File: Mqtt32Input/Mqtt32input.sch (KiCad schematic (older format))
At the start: 66 parts, among them J1 INPUT 0-7, J10 SLAVE2 IN/DATA OUTPUT, J2 JP OPT1, J3 JP OPT2, J4 INPUT 8-15, J5 INPUT 16-23, J6 SLAVE1IN/CHAIN INPUT, J7 JP CHAIN IN(1)/SLAVE1(3), J8 JP DATA OUT(1)/SLAVE2(3), J9 INPUT 24-31, SW1 DIP NODE 0-3, SW2 DIP # Chain length, U1 74HC165, U2 74HC165, U3 74HC165, U4 74HC165, X1 0V - 5V

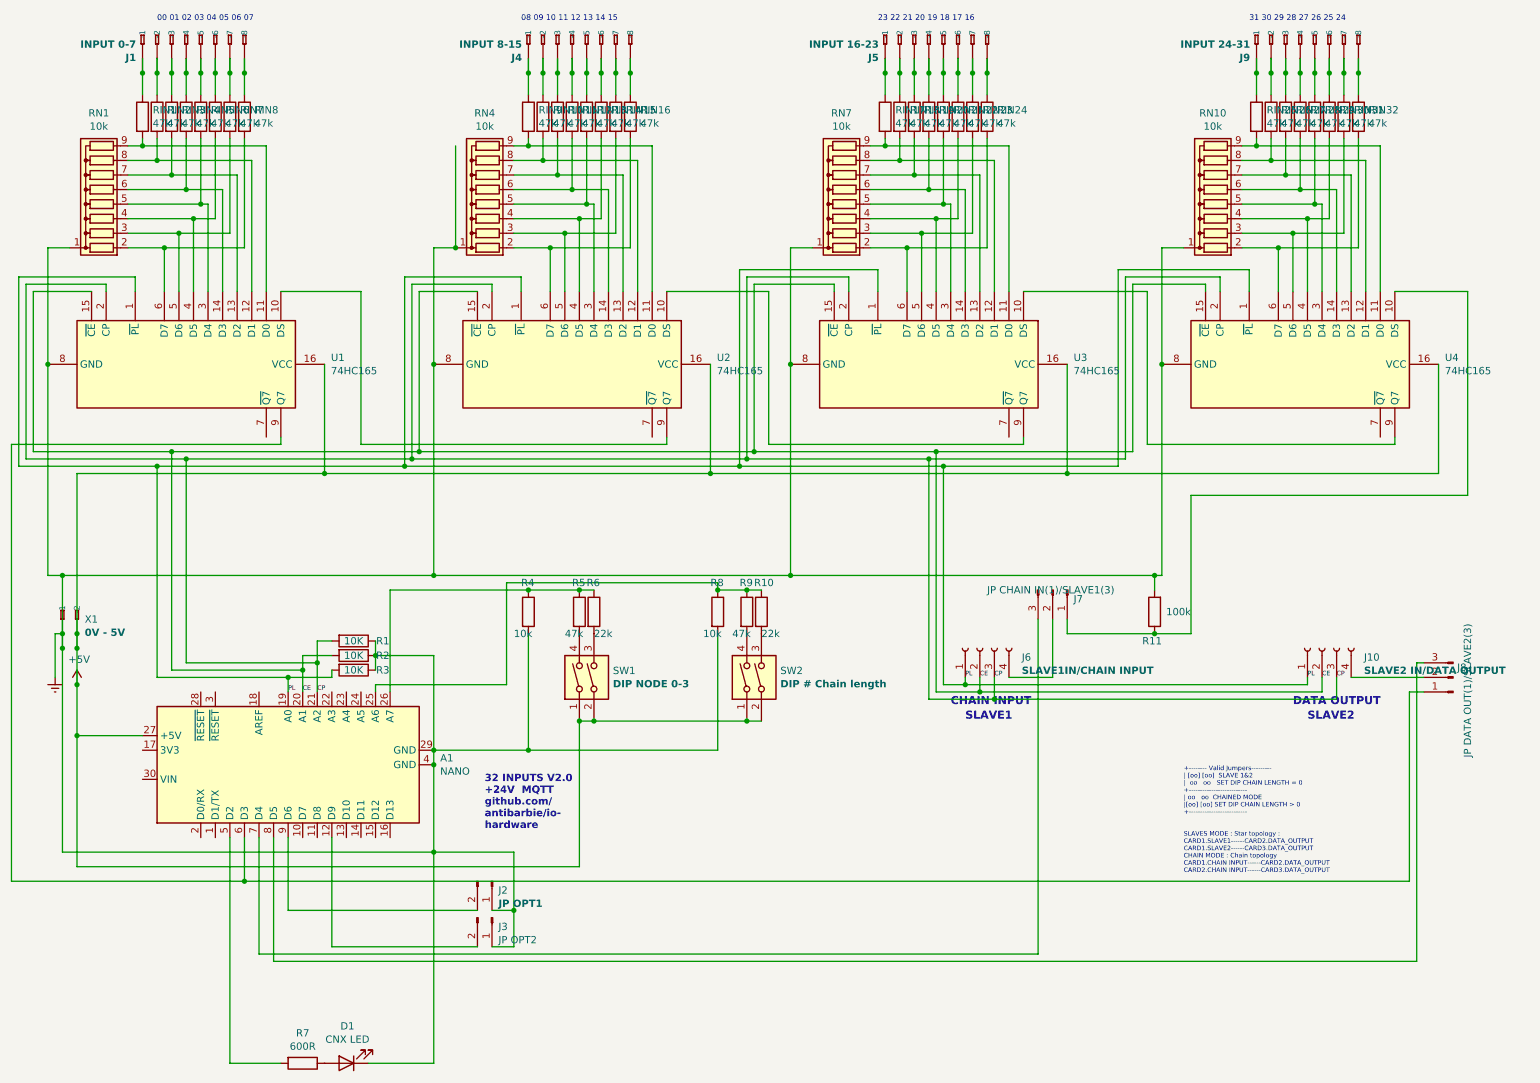
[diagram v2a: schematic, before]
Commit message: Fix comments/layout on the main schematics
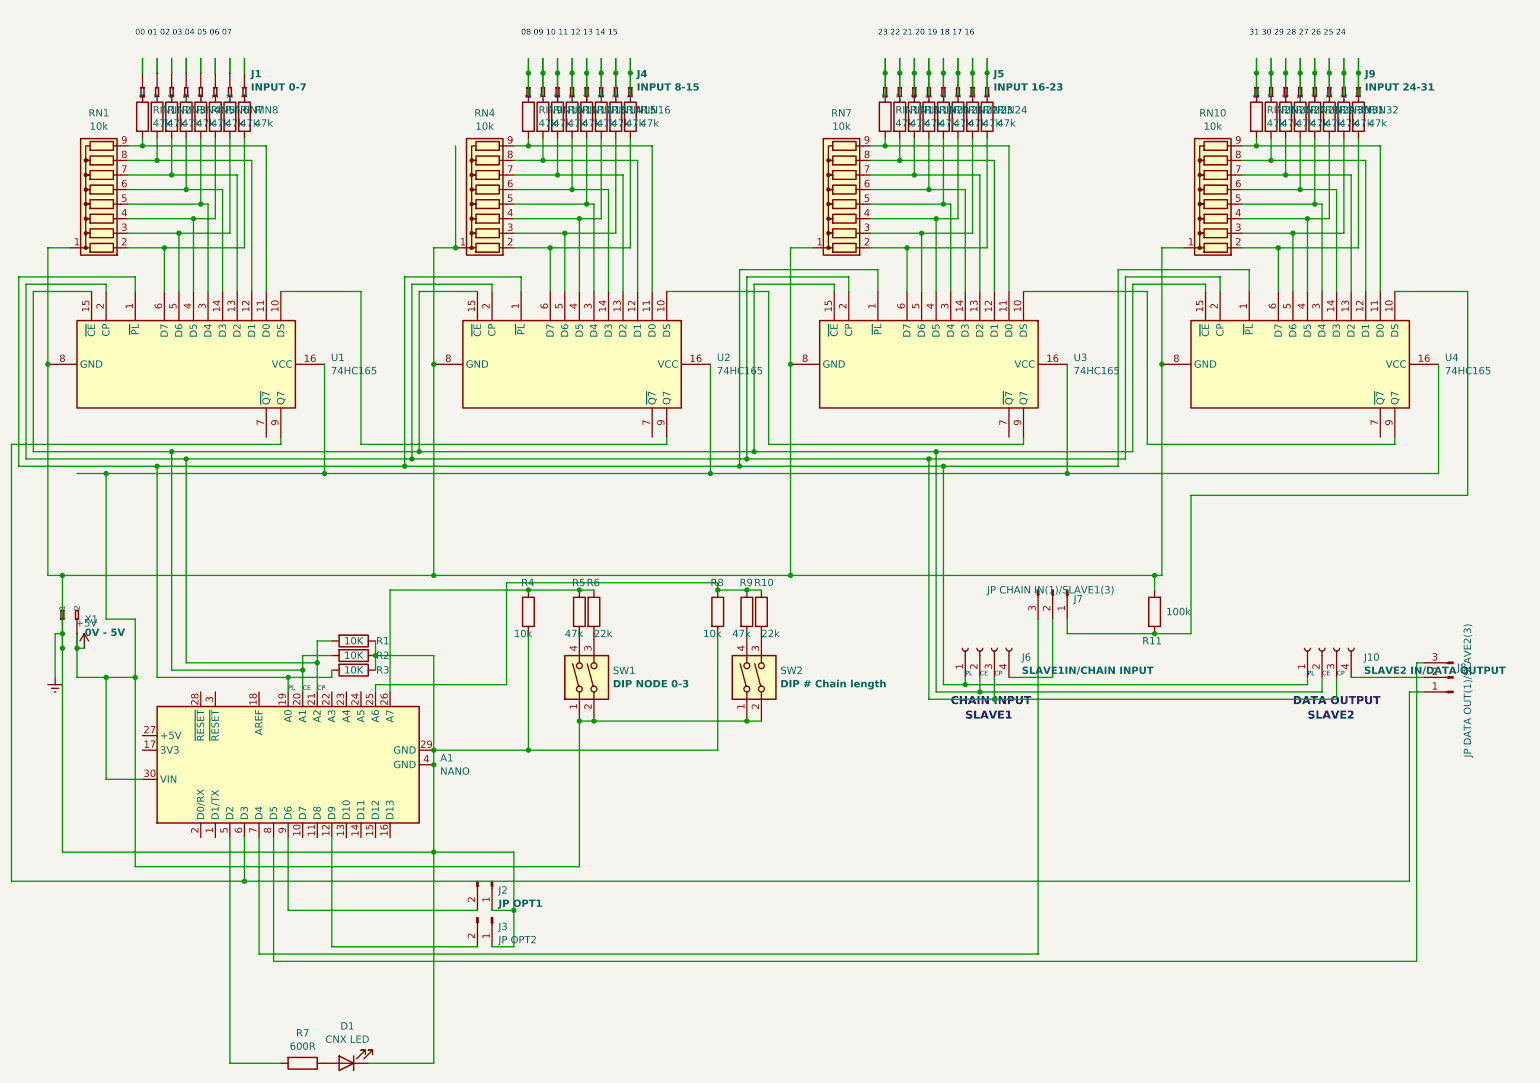
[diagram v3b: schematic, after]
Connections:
- net +5V: now also A1.30 (VIN); no longer A1.27 (+5V)
- net at J4.A1 (-1), J4.B1: now also RIN16.1; no longer RIN9.1
- net at J4.A2 (-2), J4.B2: now also RIN15.1; no longer RIN10.1
- net at J4.A3 (-3), J4.B3: now also RIN14.1; no longer RIN11.1
- net at J4.A4 (-4), J4.B4: now also RIN13.1; no longer RIN12.1
- net at J4.A5 (-5), J4.B5: now also RIN12.1; no longer RIN13.1
- net at J4.A6 (-6), J4.B6: now also RIN11.1; no longer RIN14.1
- net at J4.A7 (-7), J4.B7: now also RIN10.1; no longer RIN15.1
- net at J4.A8 (-8), J4.B8: now also RIN9.1; no longer RIN16.1
- net at J5.A1 (-1), J5.B1: now also RIN24.1; no longer RIN17.1
- net at J5.A2 (-2), J5.B2: now also RIN23.1; no longer RIN18.1
- net at J5.A3 (-3), J5.B3: now also RIN22.1; no longer RIN19.1
- net at J5.A4 (-4), J5.B4: now also RIN21.1; no longer RIN20.1
- net at J5.A5 (-5), J5.B5: now also RIN20.1; no longer RIN21.1
- net at J5.A6 (-6), J5.B6: now also RIN19.1; no longer RIN22.1
- net at J5.A7 (-7), J5.B7: now also RIN18.1; no longer RIN23.1
- net at J5.A8 (-8), J5.B8: now also RIN17.1; no longer RIN24.1
- net at J9.A1 (-1), J9.B1: now also RIN32.1; no longer RIN25.1
- net at J9.A2 (-2), J9.B2: now also RIN31.1; no longer RIN26.1
- net at J9.A3 (-3), J9.B3: now also RIN30.1; no longer RIN27.1
- net at J9.A4 (-4), J9.B4: now also RIN29.1; no longer RIN28.1
- net at J9.A5 (-5), J9.B5: now also RIN28.1; no longer RIN29.1
- net at J9.A6 (-6), J9.B6: now also RIN27.1; no longer RIN30.1
- net at J9.A7 (-7), J9.B7: now also RIN26.1; no longer RIN31.1
- net at J9.A8 (-8), J9.B8: now also RIN25.1; no longer RIN32.1
- net at J1.A1 (-1), J1.B1: no longer RIN1.1
- net at J1.A2 (-2), J1.B2: no longer RIN2.1
- net at J1.A3 (-3), J1.B3: no longer RIN3.1
- net at J1.A4 (-4), J1.B4: no longer RIN4.1
- net at J1.A5 (-5), J1.B5: no longer RIN5.1
- net at J1.A6 (-6), J1.B6: no longer RIN6.1
- net at J1.A7 (-7), J1.B7: no longer RIN7.1
- net at J1.A8 (-8), J1.B8: no longer RIN8.1
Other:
- note removed: "+-------- Valid Jumpers---------\n| [oo] [oo] SLAVE 1&2\n| oo oo SET DIP CHAIN LENGTH = 0\n+--------------------------\n| oo oo CHAINED MODE\n|[oo] [oo] SET DIP CHAIN LENGTH > 0\n+--------------------------"
- note removed: "32 INPUTS V2.0 \n+24V MQTT\ngithub.com/\nantibarbie/io-\nhardware"
- note removed: "SLAVES MODE : Star topology :\nCARD1.SLAVE1------CARD2.DATA_OUTPUT\nCARD1.SLAVE2------CARD3.DATA_OUTPUT\nCHAIN MODE : Chain topology\nCARD1.CHAIN INPUT------CARD2.DATA_OUTPUT\nCARD2.CHAIN INPUT------CARD3.DATA_OUTPUT\n"
- moved on the sheet: J1, J4, J5, J9
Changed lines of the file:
@@
 L power:+5V #PWR02
 U 1 1 5FAE756F
-P 1400 5000
-F 0 "#PWR02" H 1400 4850 50  0001 C CNN
-F 1 "+5V" H 1415 5173 50  0000 C CNN
-F 2 "" H 1400 5000 50  0001 C CNN
-F 3 "" H 1400 5000 50  0001 C CNN
-	1    1400 5000
+P 1450 4750
+F 0 "#PWR02" H 1450 4600 50  0001 C CNN
+F 1 "+5V" H 1465 4923 50  0000 C CNN
+F 2 "" H 1450 4750 50  0001 C CNN
+F 3 "" H 1450 4750 50  0001 C CNN
+	1    1450 4750
 	1    0    0    -1
 $EndComp
@@
 Connection ~ 1300 4650
 Wire Wire Line
-	1400 5350 1850 5350
-Connection ~ 1400 5000
-Wire Wire Line
-	1400 5000 1400 5350
-Wire Wire Line
 	1300 6150 3850 6150
 Wire Wire Line
@@
 Connection ~ 3050 4850
 Wire Wire Line
-	1400 5350 1400 6250
-Wire Wire Line
-	1400 6250 4850 6250
-Wire Wire Line
 	4850 6250 4850 5250
-Connection ~ 1400 5350
 Wire Wire Line
 	4850 5250 4950 5250
@@
 	0    -1   -1   0
 $EndComp
-$Comp
-L 233-508:233-508 J1
-U 1 1 5FF70C98
-P 2150 500
-F 0 "J1" V 1956 844 50  0000 L CNB
-F 1 "INPUT 0-7" V 2047 844 50  0000 L CNB
-F 2 "_Extra_footprints:233-508" H 2150 500 50  0001 L BNN
-F 3 "" H 2150 500 50  0001 L BNN
-F 4 "Wago Corporation" H 2150 500 50  0001 L BNN "MF"
-F 5 "0233-0508" H 2150 500 50  0001 L BNN "MPN"
-F 6 "79K2053" H 2150 500 50  0001 L BNN "OC_NEWARK"
-F 7 "1777101" H 2150 500 50  0001 L BNN "OC_FARNELL"
-	1    2150 500
-	0    -1   -1   0
-$EndComp
-Text Notes 4200 6000 0    50   ~ 10
-32 INPUTS V2.0 \n+24V  MQTT\ngithub.com/\nantibarbie/io-\nhardware
-Text Notes 1950 450  0    39   ~ 0
+Text Notes 1800 550  0    39   ~ 0
 00 01 02 03 04 05 06 07
-Text Notes 4450 450  0    39   ~ 0
+Text Notes 4450 550  0    39   ~ 0
 08 09 10 11 12 13 14 15
-Text Notes 6900 450  0    39   ~ 0
+Text Notes 6900 550  0    39   ~ 0
 23 22 21 20 19 18 17 16
-Text Notes 9450 450  0    39   ~ 0
+Text Notes 9450 550  0    39   ~ 0
 31 30 29 28 27 26 25 24
-Wire Wire Line
-	1400 4650 1400 4750
-Connection ~ 1400 4750
-Wire Wire Line
-	1400 4750 1400 5000
 Wire Wire Line
 	1300 4650 1300 4750
@@
 $EndComp
 Wire Wire Line
-	1850 700  1850 800
-Connection ~ 1850 800
-Connection ~ 1950 800
-Wire Wire Line
-	1950 800  1950 700
-Connection ~ 2050 800
-Wire Wire Line
-	2050 800  2050 700
-Connection ~ 2150 800
-Wire Wire Line
-	2150 800  2150 700
-Connection ~ 2250 800
-Wire Wire Line
-	2250 800  2250 700
-Connection ~ 2350 800
-Wire Wire Line
-	2350 800  2350 700
-Connection ~ 2450 800
-Wire Wire Line
-	2450 800  2450 700
-Connection ~ 2550 800
-Wire Wire Line
-	2550 800  2550 700
-Wire Wire Line
 	1750 1300 1850 1300
 Wire Wire Line
@@
 L 233-508:233-508 J4
 U 1 1 5FE04CBC
-P 4800 500
-F 0 "J4" V 4606 844 50  0000 L CNB
-F 1 "INPUT 8-15" V 4697 844 50  0000 L CNB
-F 2 "_Extra_footprints:233-508" H 4800 500 50  0001 L BNN
-F 3 "" H 4800 500 50  0001 L BNN
-F 4 "Wago Corporation" H 4800 500 50  0001 L BNN "MF"
-F 5 "0233-0508" H 4800 500 50  0001 L BNN "MPN"
-F 6 "79K2053" H 4800 500 50  0001 L BNN "OC_NEWARK"
-F 7 "1777101" H 4800 500 50  0001 L BNN "OC_FARNELL"
-	1    4800 500
-	0    -1   -1   0
+P 4900 1000
+F 0 "J4" V 4706 1344 50  0000 L CNB
+F 1 "INPUT 8-15" V 4797 1344 50  0000 L CNB
+F 2 "_Extra_footprints:233-508" H 4900 1000 50  0001 L BNN
+F 3 "" H 4900 1000 50  0001 L BNN
+F 4 "Wago Corporation" H 4900 1000 50  0001 L BNN "MF"
+F 5 "0233-0508" H 4900 1000 50  0001 L BNN "MPN"
+F 6 "79K2053" H 4900 1000 50  0001 L BNN "OC_NEWARK"
+F 7 "1777101" H 4900 1000 50  0001 L BNN "OC_FARNELL"
+	1    4900 1000
+	0    1    1    0
 $EndComp
 $Comp
@@
 L 233-508:233-508 J5
 U 1 1 5FE104B8
-P 7250 500
-F 0 "J5" V 7056 844 50  0000 L CNB
-F 1 "INPUT 16-23" V 7147 844 50  0000 L CNB
-F 2 "_Extra_footprints:233-508" H 7250 500 50  0001 L BNN
-F 3 "" H 7250 500 50  0001 L BNN
-F 4 "Wago Corporation" H 7250 500 50  0001 L BNN "MF"
-F 5 "0233-0508" H 7250 500 50  0001 L BNN "MPN"
-F 6 "79K2053" H 7250 500 50  0001 L BNN "OC_NEWARK"
-F 7 "1777101" H 7250 500 50  0001 L BNN "OC_FARNELL"
-	1    7250 500
-	0    -1   -1   0
+P 7350 1000
+F 0 "J5" V 7156 1344 50  0000 L CNB
+F 1 "INPUT 16-23" V 7247 1344 50  0000 L CNB
+F 2 "_Extra_footprints:233-508" H 7350 1000 50  0001 L BNN
+F 3 "" H 7350 1000 50  0001 L BNN
+F 4 "Wago Corporation" H 7350 1000 50  0001 L BNN "MF"
+F 5 "0233-0508" H 7350 1000 50  0001 L BNN "MPN"
+F 6 "79K2053" H 7350 1000 50  0001 L BNN "OC_NEWARK"
+F 7 "1777101" H 7350 1000 50  0001 L BNN "OC_FARNELL"
+	1    7350 1000
+	0    1    1    0
 $EndComp
 $Comp
@@
 L 233-508:233-508 J9
 U 1 1 5FE1EE35
-P 9800 500
-F 0 "J9" V 9606 844 50  0000 L CNB
-F 1 "INPUT 24-31" V 9697 844 50  0000 L CNB
-F 2 "_Extra_footprints:233-508" H 9800 500 50  0001 L BNN
-F 3 "" H 9800 500 50  0001 L BNN
-F 4 "Wago Corporation" H 9800 500 50  0001 L BNN "MF"
-F 5 "0233-0508" H 9800 500 50  0001 L BNN "MPN"
-F 6 "79K2053" H 9800 500 50  0001 L BNN "OC_NEWARK"
-F 7 "1777101" H 9800 500 50  0001 L BNN "OC_FARNELL"
-	1    9800 500
-	0    -1   -1   0
+P 9900 1000
+F 0 "J9" V 9706 1344 50  0000 L CNB
+F 1 "INPUT 24-31" V 9797 1344 50  0000 L CNB
+F 2 "_Extra_footprints:233-508" H 9900 1000 50  0001 L BNN
+F 3 "" H 9900 1000 50  0001 L BNN
+F 4 "Wago Corporation" H 9900 1000 50  0001 L BNN "MF"
+F 5 "0233-0508" H 9900 1000 50  0001 L BNN "MPN"
+F 6 "79K2053" H 9900 1000 50  0001 L BNN "OC_NEWARK"
+F 7 "1777101" H 9900 1000 50  0001 L BNN "OC_FARNELL"
+	1    9900 1000
+	0    1    1    0
 $EndComp
 $Comp
@@
 Wire Wire Line
 	8750 2300 7900 2300
-Connection ~ 1400 4650
 Wire Wire Line
 	3100 3550 5750 3550
@@
 Connection ~ 3750 3400
 Wire Wire Line
-	1400 3550 3100 3550
-Wire Wire Line
-	1400 3550 1400 4650
+	1400 3550 1600 3550
 Connection ~ 3100 3550
 Wire Wire Line
@@
 	5800 5450 5800 4650
 Connection ~ 4500 5450
-Text Notes 9000 5900 0    31   ~ 0
-+-------- Valid Jumpers---------\n| [oo] [oo]  SLAVE 1&2\n|  oo   oo   SET DIP CHAIN LENGTH = 0\n+--------------------------\n| oo   oo  CHAINED MODE\n|[oo] [oo] SET DIP CHAIN LENGTH > 0\n+--------------------------
-Text Notes 9000 6300 0    31   ~ 0
-SLAVES MODE : Star topology :\nCARD1.SLAVE1------CARD2.DATA_OUTPUT\nCARD1.SLAVE2------CARD3.DATA_OUTPUT\nCHAIN MODE : Chain topology\nCARD1.CHAIN INPUT------CARD2.DATA_OUTPUT\nCARD2.CHAIN INPUT------CARD3.DATA_OUTPUT\n
 Text Notes 7500 5250 0    55   ~ 11
 SLAVE1
@@
 	4500 800  4500 950
 Wire Wire Line
-	2550 800  2550 950
-Wire Wire Line
-	2450 800  2450 950
-Wire Wire Line
-	2350 800  2350 950
-Wire Wire Line
-	2250 800  2250 950
-Wire Wire Line
-	2150 800  2150 950
-Wire Wire Line
-	2050 800  2050 950
-Wire Wire Line
-	1950 800  1950 950
-Wire Wire Line
-	1850 800  1850 950
+	1850 700  1850 800
+Wire Wire Line
+	1950 700  1950 800
+Wire Wire Line
+	2050 700  2050 800
+Wire Wire Line
+	2150 700  2150 800
+Wire Wire Line
+	2250 700  2250 800
+Wire Wire Line
+	2350 700  2350 800
+Wire Wire Line
+	2450 700  2450 800
+Wire Wire Line
+	2550 700  2550 800
+$Comp
+L 233-508:233-508 J1
+U 1 1 5FF70C98
+P 2250 1000
+F 0 "J1" V 2056 1344 50  0000 L CNB
+F 1 "INPUT 0-7" V 2147 1344 50  0000 L CNB
+F 2 "_Extra_footprints:233-508" H 2250 1000 50  0001 L BNN
+F 3 "" H 2250 1000 50  0001 L BNN
+F 4 "Wago Corporation" H 2250 1000 50  0001 L BNN "MF"
+F 5 "0233-0508" H 2250 1000 50  0001 L BNN "MPN"
+F 6 "79K2053" H 2250 1000 50  0001 L BNN "OC_NEWARK"
+F 7 "1777101" H 2250 1000 50  0001 L BNN "OC_FARNELL"
+	1    2250 1000
+	0    1    1    0
+$EndComp
+Wire Wire Line
+	1450 4750 1400 4750
+Wire Wire Line
+	1400 4650 1400 4750
+Connection ~ 1400 4750
+Wire Wire Line
+	1800 4550 1600 4550
+Wire Wire Line
+	1600 4550 1600 3550
+Connection ~ 1600 3550
+Wire Wire Line
+	1600 3550 3100 3550
+Wire Wire Line
+	1600 4950 1600 5650
+Wire Wire Line
+	1600 5650 1850 5650
+Wire Wire Line
+	1800 6250 4850 6250
+Wire Wire Line
+	1800 4550 1800 4950
+Wire Wire Line
+	1400 4750 1400 4950
+Wire Wire Line
+	1400 4950 1600 4950
+Wire Wire Line
+	1600 4950 1800 4950
+Connection ~ 1600 4950
+Connection ~ 1800 4950
+Wire Wire Line
+	1800 4950 1800 6250
 $EndSCHEMATC
